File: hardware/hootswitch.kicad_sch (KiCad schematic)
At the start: 66 parts, among them J1 Mini-DIN-4-G, J10 POWSEL, J11 TWI, J12 TWI, J2 Mini-DIN-4-G, J7 Barrel_Jack_MountingPin, J8 EXT_POW, J9 SW1, Q1 MMBT3904, Q2 MMBT3904, Q3 MMBT3904, Q4 MMBT3904, Q5 MMBT3904, Q6 MMBT3904, Q7 MMBT3904, Q8 MMBT3904, SW1 Switch1, U1 PicoW, U2 LM1117-5.0, U7 ADuM1201AR

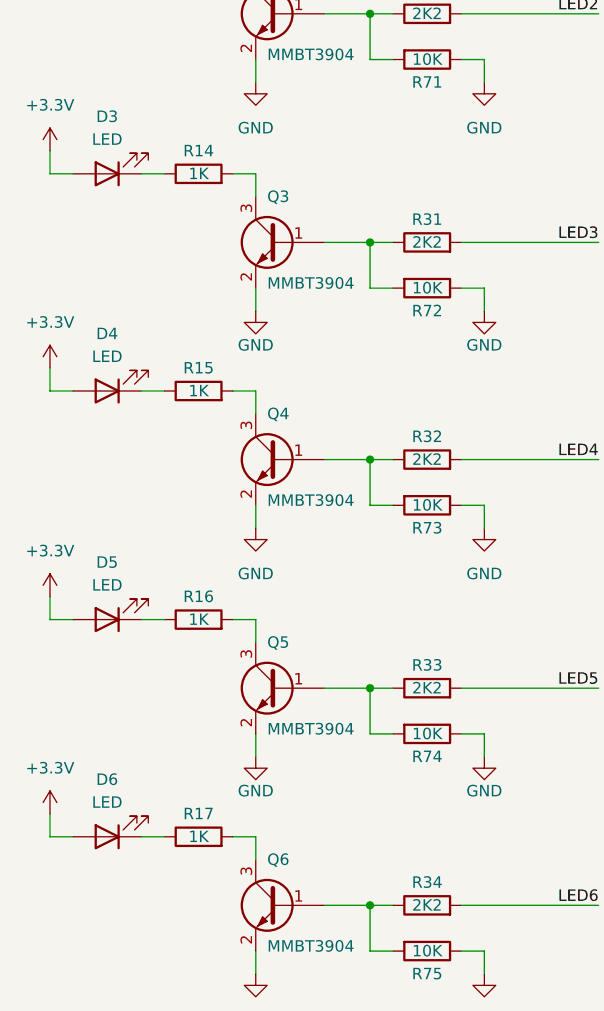
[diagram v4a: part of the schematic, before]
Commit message: Increase resistance for the green LEDs
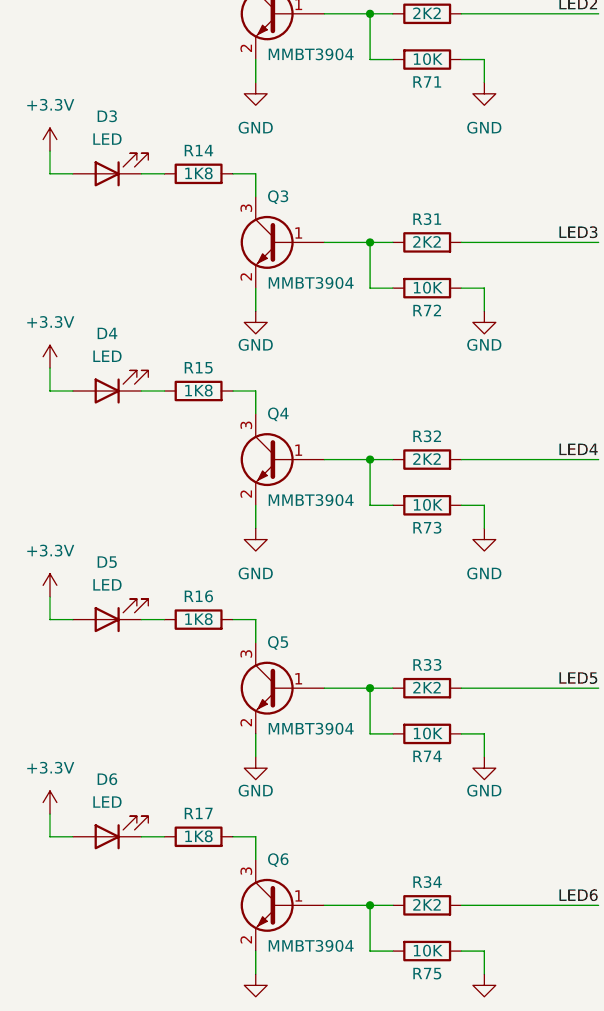
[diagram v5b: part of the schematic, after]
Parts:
- R14, R15, R16, R17: value 1K -> 1K8
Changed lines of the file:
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@@
     (in_bom yes) (on_board yes)
     (property "Reference" "R17" (id 0) (at 36.83 146.05 90))
-    (property "Value" "1K" (id 1) (at 36.83 148.59 90))
+    (property "Value" "1K8" (id 1) (at 36.83 148.59 90))
     (property "Footprint" "Resistor_SMD:R_0603_1608Metric" (id 2) (at 36.83 150.368 90)
       (effects (font (size 1.27 1.27)) hide)
@@
     (in_bom yes) (on_board yes)
     (property "Reference" "R15" (id 0) (at 36.83 96.52 90))
-    (property "Value" "1K" (id 1) (at 36.83 99.06 90))
+    (property "Value" "1K8" (id 1) (at 36.83 99.06 90))
     (property "Footprint" "Resistor_SMD:R_0603_1608Metric" (id 2) (at 36.83 100.838 90)
       (effects (font (size 1.27 1.27)) hide)
@@
     (in_bom yes) (on_board yes)
     (property "Reference" "R16" (id 0) (at 36.83 121.92 90))
-    (property "Value" "1K" (id 1) (at 36.83 124.46 90))
+    (property "Value" "1K8" (id 1) (at 36.83 124.46 90))
     (property "Footprint" "Resistor_SMD:R_0603_1608Metric" (id 2) (at 36.83 126.238 90)
       (effects (font (size 1.27 1.27)) hide)
@@
     (in_bom yes) (on_board yes)
     (property "Reference" "R14" (id 0) (at 36.83 72.39 90))
-    (property "Value" "1K" (id 1) (at 36.83 74.93 90))
+    (property "Value" "1K8" (id 1) (at 36.83 74.93 90))
     (property "Footprint" "Resistor_SMD:R_0603_1608Metric" (id 2) (at 36.83 76.708 90)
       (effects (font (size 1.27 1.27)) hide)
@@
     )
     (path "/5faba3b4-7252-457e-806b-093f5571761d"
-      (reference "R14") (unit 1) (value "1K") (footprint "Resistor_SMD:R_0603_1608Metric")
+      (reference "R14") (unit 1) (value "1K8") (footprint "Resistor_SMD:R_0603_1608Metric")
     )
     (path "/4a5fef5c-975e-4ae3-913d-b760655bf213"
-      (reference "R15") (unit 1) (value "1K") (footprint "Resistor_SMD:R_0603_1608Metric")
+      (reference "R15") (unit 1) (value "1K8") (footprint "Resistor_SMD:R_0603_1608Metric")
     )
     (path "/4f5d9dd0-f536-40f3-96ab-963fb2c2f665"
-      (reference "R16") (unit 1) (value "1K") (footprint "Resistor_SMD:R_0603_1608Metric")
+      (reference "R16") (unit 1) (value "1K8") (footprint "Resistor_SMD:R_0603_1608Metric")
     )
     (path "/010a005f-9bb7-4e2d-97fa-5da15d0f622c"
-      (reference "R17") (unit 1) (value "1K") (footprint "Resistor_SMD:R_0603_1608Metric")
+      (reference "R17") (unit 1) (value "1K8") (footprint "Resistor_SMD:R_0603_1608Metric")
     )
     (path "/496d9e94-0c96-482e-96ba-4fa40cf02c6f/4db8d270-1bfb-4cb7-bba7-dd056505ff5c"

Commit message: Increase mounting hole size to support M3 screws.
These will require small head screws, they are very close to other items. This may require further board modifications.
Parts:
- H1, H2, H3, H4: footprint MountingHole:MountingHole_2.7mm_M2.5 -> MountingHole:MountingHole_3.2mm_M3
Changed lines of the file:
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@@
       (effects (font (size 1.27 1.27)) (justify left))
     )
-    (property "Footprint" "MountingHole:MountingHole_2.7mm_M2.5" (id 2) (at 190.5 222.25 0)
+    (property "Footprint" "MountingHole:MountingHole_3.2mm_M3" (id 2) (at 190.5 222.25 0)
       (effects (font (size 1.27 1.27)) hide)
     )
@@
       (effects (font (size 1.27 1.27)) (justify left))
     )
-    (property "Footprint" "MountingHole:MountingHole_2.7mm_M2.5" (id 2) (at 190.5 209.55 0)
+    (property "Footprint" "MountingHole:MountingHole_3.2mm_M3" (id 2) (at 190.5 209.55 0)
       (effects (font (size 1.27 1.27)) hide)
     )
@@
       (effects (font (size 1.27 1.27)) (justify left))
     )
-    (property "Footprint" "MountingHole:MountingHole_2.7mm_M2.5" (id 2) (at 190.5 228.6 0)
+    (property "Footprint" "MountingHole:MountingHole_3.2mm_M3" (id 2) (at 190.5 228.6 0)
       (effects (font (size 1.27 1.27)) hide)
     )
@@
       (effects (font (size 1.27 1.27)) (justify left))
     )
-    (property "Footprint" "MountingHole:MountingHole_2.7mm_M2.5" (id 2) (at 190.5 215.9 0)
+    (property "Footprint" "MountingHole:MountingHole_3.2mm_M3" (id 2) (at 190.5 215.9 0)
       (effects (font (size 1.27 1.27)) hide)
     )
@@
     )
     (path "/c340a452-9756-4c08-8734-2a2cc26b8d0c"
-      (reference "H1") (unit 1) (value "M") (footprint "MountingHole:MountingHole_2.7mm_M2.5")
+      (reference "H1") (unit 1) (value "M") (footprint "MountingHole:MountingHole_3.2mm_M3")
     )
     (path "/cab999c8-adde-436d-8532-822f034b143b"
-      (reference "H2") (unit 1) (value "M") (footprint "MountingHole:MountingHole_2.7mm_M2.5")
+      (reference "H2") (unit 1) (value "M") (footprint "MountingHole:MountingHole_3.2mm_M3")
     )
     (path "/39bfef16-736d-4f73-90e0-a6e99e8e1231"
-      (reference "H3") (unit 1) (value "M") (footprint "MountingHole:MountingHole_2.7mm_M2.5")
+      (reference "H3") (unit 1) (value "M") (footprint "MountingHole:MountingHole_3.2mm_M3")
     )
     (path "/c8399a09-8d79-440c-b466-2678dfc0044f"
-      (reference "H4") (unit 1) (value "M") (footprint "MountingHole:MountingHole_2.7mm_M2.5")
+      (reference "H4") (unit 1) (value "M") (footprint "MountingHole:MountingHole_3.2mm_M3")
     )
     (path "/dc696315-f7be-4ce8-acd7-3e1a0e1b9cc8"

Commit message: Hardware 2024c.
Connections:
- net GND: now also J7.2, J8.2 (Pin_2)
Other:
- moved on the sheet: J7
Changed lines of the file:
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@@
   (junction (at 53.34 193.04) (diameter 0) (color 0 0 0 0)
   )
+  (junction (at 116.84 36.83) (diameter 0) (color 0 0 0 0)
+  )
   (junction (at 35.56 223.52) (diameter 0) (color 0 0 0 0)
   )
@@
   (no_connect (at 151.13 67.31))
   (no_connect (at 130.81 113.03))
-  (no_connect (at 109.22 41.91))
+  (no_connect (at 106.68 41.91))
   (no_connect (at 151.13 72.39))
   (no_connect (at 27.94 213.36))
@@
     (stroke (width 0) (type default) (color 0 0 0 0))
   )
-  (wire (pts (xy 116.84 31.75) (xy 125.73 31.75))
+  (wire (pts (xy 114.3 31.75) (xy 125.73 31.75))
     (stroke (width 0) (type default) (color 0 0 0 0))
   )
@@
     (stroke (width 0) (type default) (color 0 0 0 0))
   )
+  (wire (pts (xy 116.84 36.83) (xy 116.84 41.91))
+    (stroke (width 0) (type default) (color 0 0 0 0))
+  )
   (wire (pts (xy 168.91 100.33) (xy 151.13 100.33))
     (stroke (width 0) (type default) (color 0 0 0 0))
@@
     (stroke (width 0) (type default) (color 0 0 0 0))
   )
-  (wire (pts (xy 116.84 36.83) (xy 123.19 36.83))
+  (wire (pts (xy 114.3 36.83) (xy 116.84 36.83))
     (stroke (width 0) (type default) (color 0 0 0 0))
   )
@@
     (stroke (width 0) (type default) (color 0 0 0 0))
   )
+  (wire (pts (xy 116.84 36.83) (xy 123.19 36.83))
+    (stroke (width 0) (type default) (color 0 0 0 0))
+  )
   (wire (pts (xy 113.03 102.87) (xy 115.57 102.87))
     (stroke (width 0) (type default) (color 0 0 0 0))
@@
     (pin "1")
   )
+  (symbol (lib_id "power:GND") (at 116.84 41.91 0) (unit 1)
+    (in_bom yes) (on_board yes) (fields_autoplaced)
+    (property "Reference" "#PWR?" (id 0) (at 116.84 48.26 0)
+      (effects (font (size 1.27 1.27)) hide)
+    )
+    (property "Value" "GND" (id 1) (at 116.84 46.99 0))
+    (property "Footprint" "" (id 2) (at 116.84 41.91 0)
+      (effects (font (size 1.27 1.27)) hide)
+    )
+    (property "Datasheet" "" (id 3) (at 116.84 41.91 0)
+      (effects (font (size 1.27 1.27)) hide)
+    )
+    (pin "1")
+  )
   (symbol (lib_id "Isolator:ADuM1201AR") (at 104.14 198.12 0) (mirror y) (unit 1)
     (in_bom yes) (on_board yes) (fields_autoplaced)
@@
     (pin "3")
   )
-  (symbol (lib_id "Connector:Barrel_Jack_MountingPin") (at 109.22 34.29 0) (unit 1)
+  (symbol (lib_id "Connector:Barrel_Jack_MountingPin") (at 106.68 34.29 0) (unit 1)
     (in_bom yes) (on_board yes) (fields_autoplaced)
-    (property "Reference" "J7" (id 0) (at 109.22 25.4 0))
-    (property "Value" "Barrel_Jack_MountingPin" (id 1) (at 109.22 27.94 0))
-    (property "Footprint" "Connector_BarrelJack:BarrelJack_CUI_PJ-063AH_Horizontal_CircularHoles" (id 2) (at 110.49 35.306 0)
+    (property "Reference" "J7" (id 0) (at 106.68 25.4 0))
+    (property "Value" "Barrel_Jack_MountingPin" (id 1) (at 106.68 27.94 0))
+    (property "Footprint" "Connector_BarrelJack:BarrelJack_CUI_PJ-063AH_Horizontal_CircularHoles" (id 2) (at 107.95 35.306 0)
       (effects (font (size 1.27 1.27)) hide)
     )
-    (property "Datasheet" "~" (id 3) (at 110.49 35.306 0)
+    (property "Datasheet" "~" (id 3) (at 107.95 35.306 0)
       (effects (font (size 1.27 1.27)) hide)
     )
@@
       (reference "#PWR0169") (unit 1) (value "GND") (footprint "")
     )
+    (path "/ae54d181-9a61-4bee-898b-047b8616a17e"
+      (reference "#PWR?") (unit 1) (value "GND") (footprint "")
+    )
     (path "/6257e51e-b774-4a5c-8ba4-62c83477bcc7"
